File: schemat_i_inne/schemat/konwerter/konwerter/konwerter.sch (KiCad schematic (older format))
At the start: 10 parts, among them J1 Conn_01x04_Male, J2 Conn_01x04_Male, U1 IRF7476, U3 IRF7476, U4 IRF7476

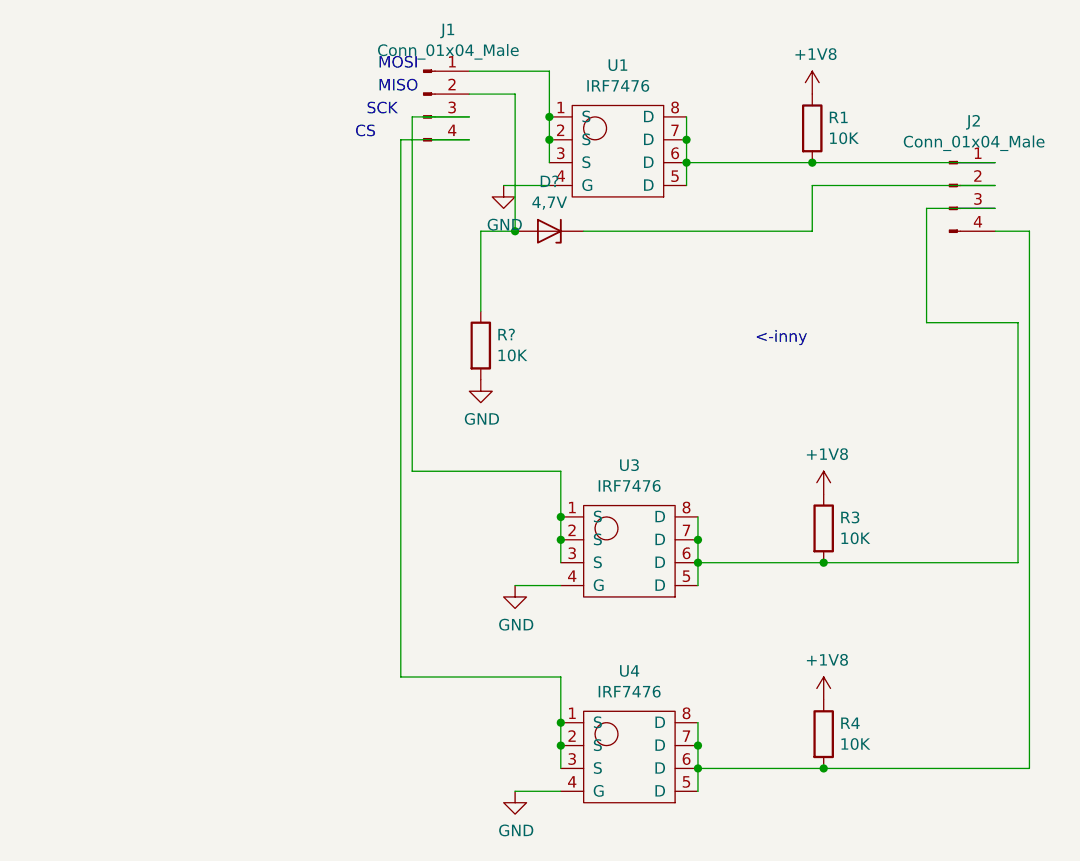
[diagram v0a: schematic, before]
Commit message: Poprawiony wyglad konwertera
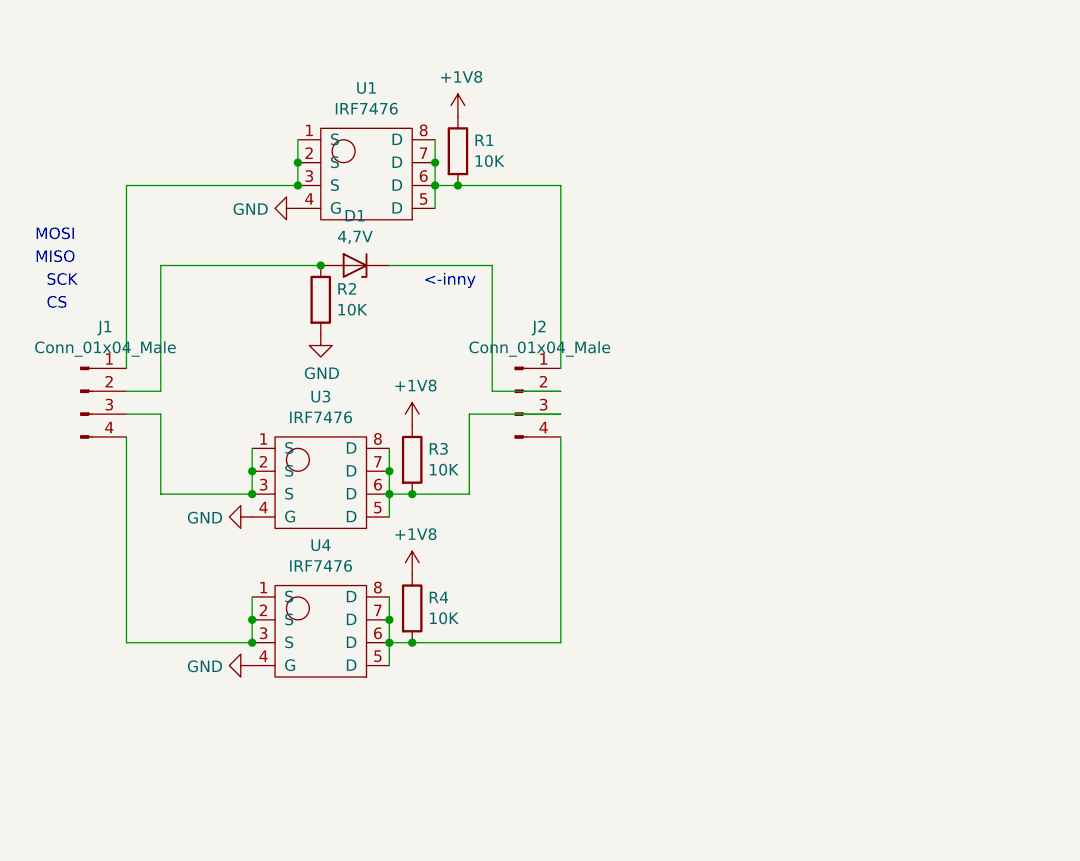
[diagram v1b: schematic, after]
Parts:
- gave numbers to parts that had none: 2
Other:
- moved on the sheet: D1, J1, J2, R1, R2, R3, R4, U1, U3, U4

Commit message: Gotowa plytka karty z konwerterem
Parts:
- removed J1, J2: Conn_01x04_Male, symbol Connector:Conn_01x04_Male
- added C1, C2: 100N, Connector_PinHeader_2.54mm:PinHeader_1x02_P2.54mm_Vertical, symbol Device:C
- added J1: Conn_01x06_Male, Connector_PinHeader_2.54mm:PinHeader_1x06_P2.54mm_Vertical, symbol Connector:Conn_01x06_Male
- added J3: Micro_SD_Card, Connector_Card:SD_Kyocera_145638009511859+, symbol Connector:Micro_SD_Card
- added U2: LM1117-1.8, Package_TO_SOT_SMD:SOT-223-3_TabPin2, symbol Regulator_Linear:LM1117-1.8
- D1: footprint (none) -> Diode_THT:D_DO-41_SOD81_P7.62mm_Horizontal
- R1, R2, R3, R4: footprint (none) -> Resistor_SMD:R_0805_2012Metric_Pad1.15x1.40mm_HandSolder
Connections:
- net +1V8: now also C2.1, J3.4 (VDD), J3.7 (DAT0), U2.2 (VO)
- net GND: now also C1.2, C2.2, J1.6 (Pin_6), U2.1 (GND)
- net MOSI: now reaches U1.1 (S), U1.2 (S), U1.3 (S)
- net MOSI: now also J1.3 (Pin_3)
- net at R1.2, U1.5 (D), U1.6 (D)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: now also J3.3 (CMD)
- net MISO: now reaches D1.2 (A), R2.1
- net MISO: now also J1.5 (Pin_5)
- net SCK: now reaches U3.1 (S), U3.2 (S), U3.3 (S)
- net SCK: now also J1.4 (Pin_4)
- net CS: now reaches U4.1 (S), U4.2 (S), U4.3 (S)
- net CS: now also J1.2 (Pin_2)
- net at D1.1 (K): now also J3.8 (DAT1)
- net at R3.2, U3.5 (D), U3.6 (D)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: now also J3.6 (VSS)
- net at R4.2, U4.5 (D), U4.6 (D)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: now also J3.2 (DAT3/CD)
- new net +5V: C1.1, J1.1 (Pin_1), J3.5 (CLK), U2.3 (VI)
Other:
- note added: "+3,3V\n"
- note added: "+5V\n"
- note added: "GND"
- note added: "MOSI\n"
- note added: "Stabilizacja 1,8V\n"
- note added: "UWAGA! w tym miejscu ma być zwykła karta a nie micro, \nużyto schematu micro ze względu na niezgodność footprintu"
- note removed: "MOSI"

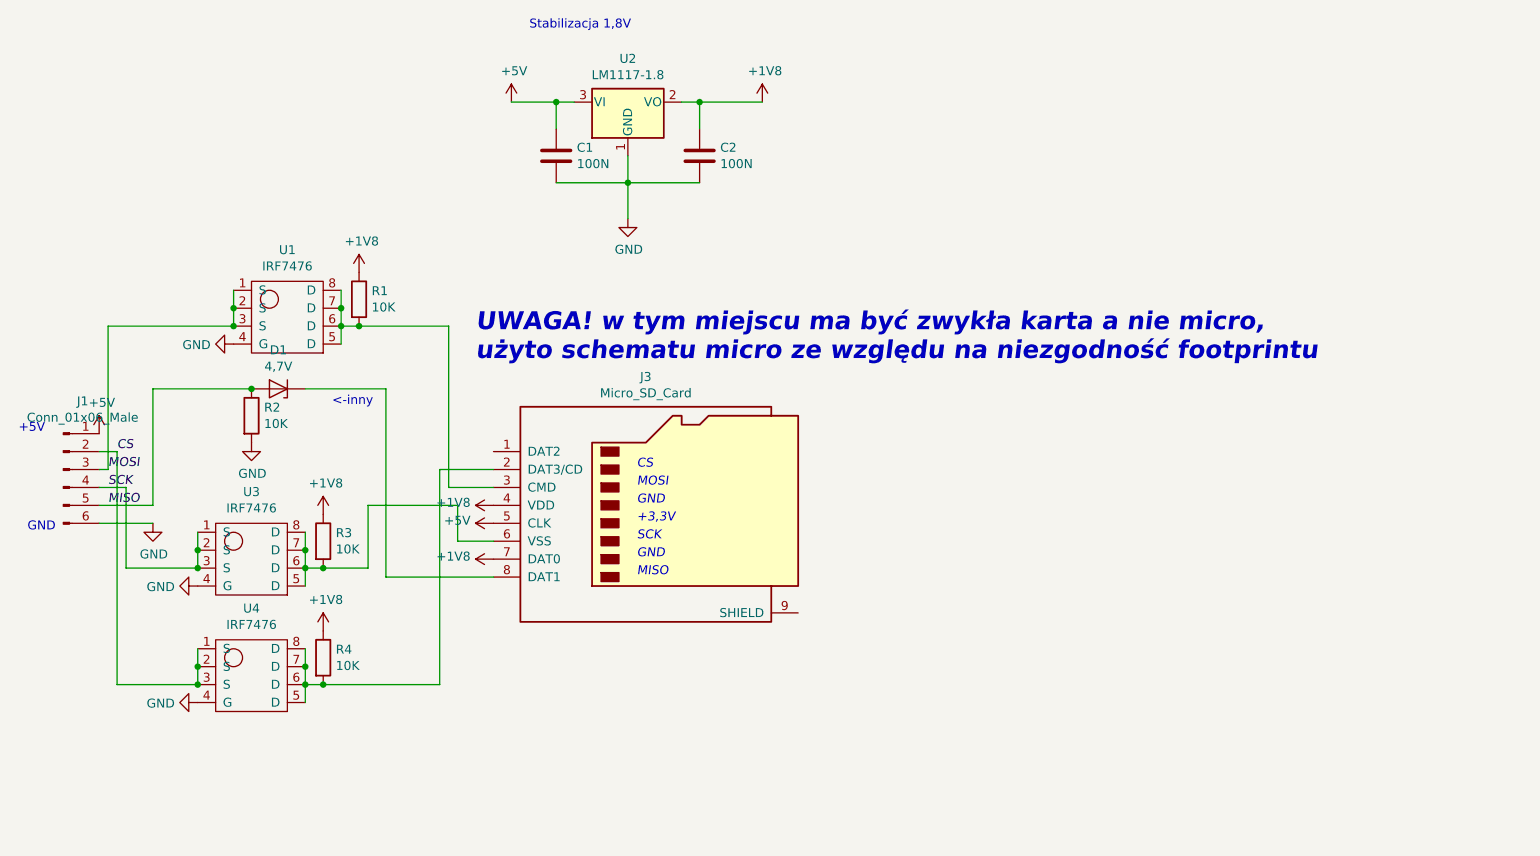
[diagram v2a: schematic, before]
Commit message: Konwerter update
-> Poprawiony schemat konwertera
-> Samodzielna płytka z konwerterem
-> poprawiony symbol karty aby pasował do footprintu
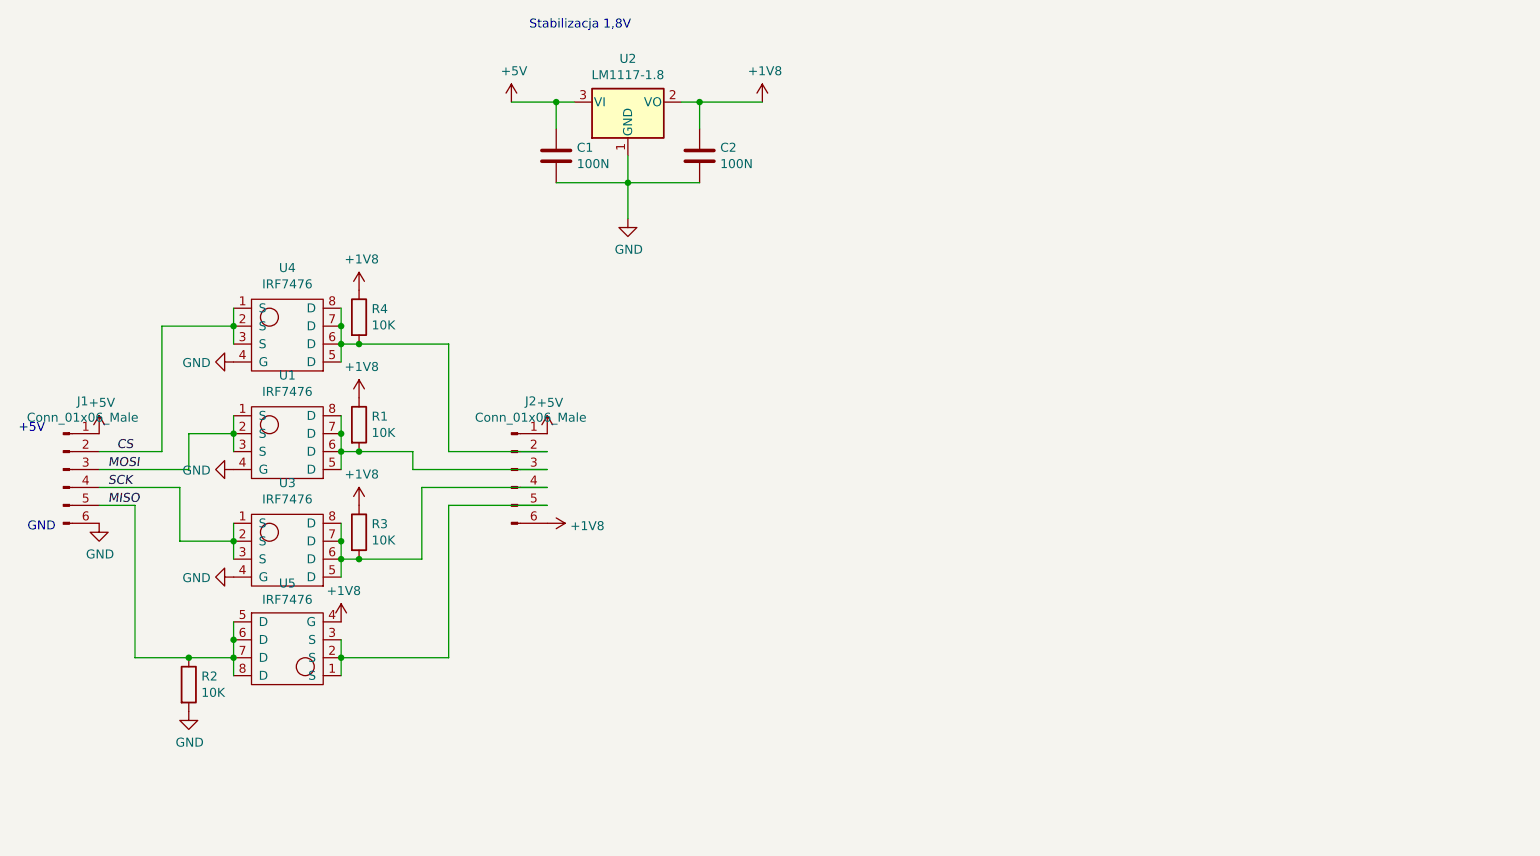
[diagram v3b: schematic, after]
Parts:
- removed D1: 4,7V, Diode_THT:D_DO-41_SOD81_P7.62mm_Horizontal, symbol Device:D_Zener
- removed J3: Micro_SD_Card, Connector_Card:SD_Kyocera_145638009511859+, symbol Connector:Micro_SD_Card
- added J2: Conn_01x06_Male, Connector_PinHeader_2.54mm:PinHeader_1x06_P2.54mm_Vertical, symbol Connector:Conn_01x06_Male
- added U5: IRF7476, Package_SO:PowerIntegrations_SO-8, symbol Device:IRF7476
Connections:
- net +1V8: now also J2.6 (Pin_6), U5.4 (G)
- net +5V: now also J2.1 (Pin_1)
- net MISO: now also U5.5 (D), U5.6 (D), U5.7 (D), U5.8 (D)
- net at R1.2, U1.5 (D), U1.6 (D)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: now also J2.3 (Pin_3)
- net at R3.2, U3.5 (D), U3.6 (D)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: now also J2.4 (Pin_4)
- net at R4.2, U4.5 (D), U4.6 (D)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: now also J2.2 (Pin_2)
- new net: J2.5 (Pin_5), U5.1 (S), U5.2 (S), U5.3 (S)
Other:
- note removed: "+3,3V\n"
- note removed: "<-inny\n"
- note removed: "CS"
- note removed: "MISO"
- note removed: "MOSI\n"
- note removed: "SCK"
- note removed: "UWAGA! w tym miejscu ma być zwykła karta a nie micro, \nużyto schematu micro ze względu na niezgodność footprintu"
- moved on the sheet: R1, R3, R4, U1, U3, U4
